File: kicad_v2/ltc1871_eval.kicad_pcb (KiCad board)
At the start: 2 copper layers, 50 x 50 mm, 40 parts, among them P9 GND, Q1 PSMN013-80YS, U1 LTC1871, U2 CSD16323Q3

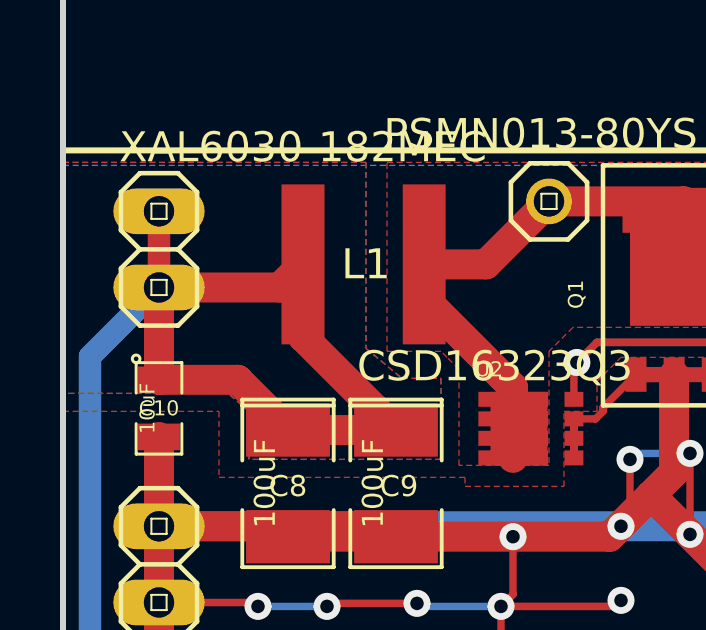
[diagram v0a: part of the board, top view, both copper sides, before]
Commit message: updated power board schematic (new RF transceiver, updated kill switch circuit, watchdog, buzzer, buttons)
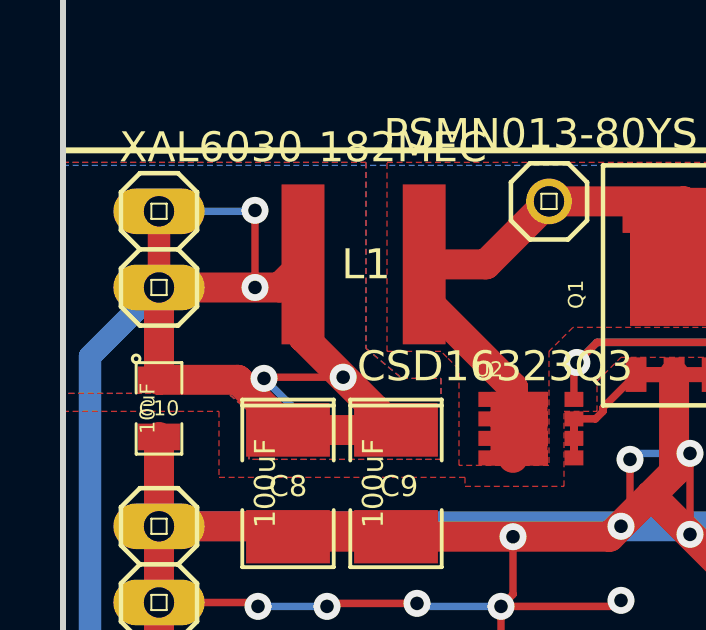
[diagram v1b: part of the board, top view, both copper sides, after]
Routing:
- net +BATT: track 47.2 -> 57.8 mm, vias 0 -> 4
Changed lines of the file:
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@@
     (thickness 1.6)
     (drawings 7)
-    (tracks 295)
+    (tracks 309)
     (zones 0)
     (modules 40)
@@
   (layers
     (15 F.Cu signal hide)
-    (0 B.Cu signal)
+    (0 B.Cu signal hide)
     (16 B.Adhes user)
     (17 F.Adhes user)
@@
     (visible_elements FFFEFFFF)
     (pcbplotparams
-      (layerselection 3178497)
+      (layerselection 536838145)
       (usegerberextensions true)
       (excludeedgelayer true)
@@
       (psa4output false)
       (plotreference true)
-      (plotvalue true)
+      (plotvalue false)
       (plotothertext true)
       (plotinvisibletext false)
@@
       (outputformat 1)
       (mirror false)
-      (drillshape 1)
+      (drillshape 0)
       (scaleselection 1)
-      (outputdirectory ""))
+      (outputdirectory /home/ken/Documents/nasa/superball/tensegrity-powerboard/kicad_v2/gebers))
   )
   (net 0 "")
@@
   (gr_line (start 61.8 11.8) (end 61.8 61.8) (angle 90) (layer Edge.Cuts) (width 0.2))
   (gr_line (start 11.8 11.8) (end 61.8 11.8) (angle 90) (layer Edge.Cuts) (width 0.2))
+  (segment (start 15 38.83) (end 18.17 38.83) (width 0.25) (layer B.Cu) (net 1) (status 400000))
+  (segment (start 18.2 41.37) (end 18.2 41.4) (width 0.25) (layer B.Cu) (net 1))
+  (via (at 18.2 41.37) (size 0.9) (layers F.Cu B.Cu) (net 1))
+  (segment (start 18.2 38.8) (end 18.2 41.37) (width 0.25) (layer F.Cu) (net 1))
+  (via (at 18.2 38.8) (size 0.9) (layers F.Cu B.Cu) (net 1))
+  (segment (start 18.17 38.83) (end 18.2 38.8) (width 0.25) (layer B.Cu) (net 1))
+  (segment (start 19.4 46.1) (end 19.4 45.3) (width 0.25) (layer B.Cu) (net 1))
+  (segment (start 21.1 44.322) (end 21.1 44.3) (width 0.25) (layer B.Cu) (net 1))
+  (segment (start 21.139 44.361) (end 21.1 44.322) (width 0.25) (layer B.Cu) (net 1))
+  (via (at 21.139 44.361) (size 0.9) (layers F.Cu B.Cu) (net 1))
+  (segment (start 18.539 44.361) (end 21.139 44.361) (width 0.25) (layer F.Cu) (net 1))
+  (segment (start 18.5 44.4) (end 18.539 44.361) (width 0.25) (layer F.Cu) (net 1))
+  (via (at 18.5 44.4) (size 0.9) (layers F.Cu B.Cu) (net 1))
+  (segment (start 19.4 45.3) (end 18.5 44.4) (width 0.25) (layer B.Cu) (net 1))
   (segment (start 19.8 40.6) (end 19.8 43.022) (width 1) (layer F.Cu) (net 1))
   (segment (start 19.8 43.022) (end 22.9 46.122) (width 1) (layer F.Cu) (net 1))
